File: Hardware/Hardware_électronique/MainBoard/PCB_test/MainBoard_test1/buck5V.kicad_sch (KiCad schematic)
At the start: 12 parts

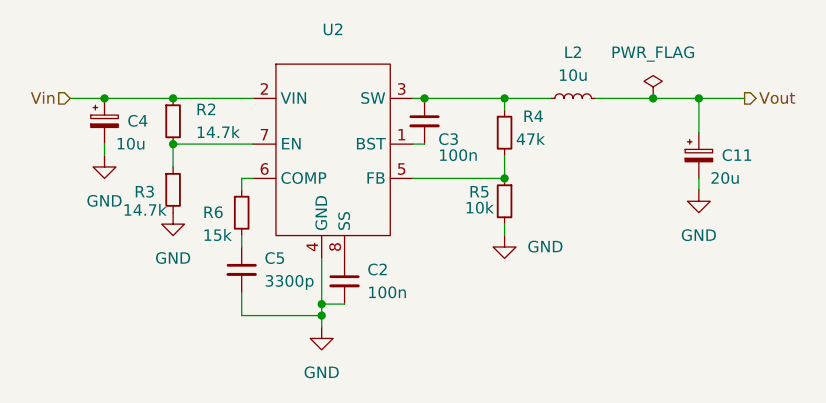
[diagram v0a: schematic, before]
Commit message: finished schematics missing footprints
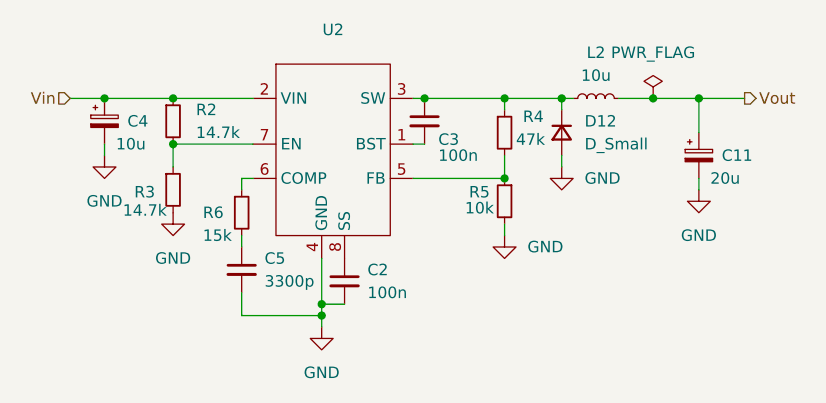
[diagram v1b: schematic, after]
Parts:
- added D12: D_Small, Diode_SMD:D_0603_1608Metric_Pad1.05x0.95mm_HandSolder, symbol Device:D_Small
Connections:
- net GND: now also D12.2 (A)
- net at C3.1, L2.1, R4.1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: now also D12.1 (K)
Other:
- moved on the sheet: L2
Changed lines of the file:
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@@
+	)
+	(junction
+		(at 121.92 63.5)
+		(diameter 0)
+		(color 0 0 0 0)
 	)
 	(junction
@@
 	(wire
 		(pts
+			(xy 121.92 71.12) (xy 121.92 69.85)
+		)
+		(stroke
+			(width 0)
+			(type default)
+		)
+	)
+	(wire
+		(pts
 			(xy 95.25 87.63) (xy 95.25 88.9)
 		)
@@
 	(wire
 		(pts
+			(xy 121.92 64.77) (xy 121.92 63.5)
+		)
+		(stroke
+			(width 0)
+			(type default)
+		)
+	)
+	(wire
+		(pts
 			(xy 105.41 72.39) (xy 115.57 72.39)
 		)
@@
 	(wire
 		(pts
+			(xy 121.92 63.5) (xy 123.19 63.5)
+		)
+		(stroke
+			(width 0)
+			(type default)
+		)
+	)
+	(wire
+		(pts
 			(xy 137.16 73.66) (xy 137.16 72.39)
 		)
@@
 	(wire
 		(pts
-			(xy 115.57 63.5) (xy 120.65 63.5)
+			(xy 115.57 63.5) (xy 121.92 63.5)
 		)
 		(stroke
@@
 	(wire
 		(pts
-			(xy 125.73 63.5) (xy 132.08 63.5)
+			(xy 128.27 63.5) (xy 132.08 63.5)
 		)
 		(stroke
@@
 	(symbol
 		(lib_id "Device:L_Small")
-		(at 123.19 63.5 90)
+		(at 125.73 63.5 90)
 		(unit 1)
 		(exclude_from_sim no)
@@
 		(fields_autoplaced yes)
 		(property "Reference" "L2"
-			(at 123.19 58.42 90)
+			(at 125.73 58.42 90)
 			(effects
 				(font
@@
 		)
 		(property "Value" "10u"
-			(at 123.19 60.96 90)
+			(at 125.73 60.96 90)
 			(effects
 				(font
@@
 		)
 		(property "Footprint" "Inductor_SMD:L_Changjiang_FNR8065S"
-			(at 123.19 63.5 0)
+			(at 125.73 63.5 0)
 			(effects
 				(font
@@
 		)
 		(property "Datasheet" "~"
-			(at 123.19 63.5 0)
+			(at 125.73 63.5 0)
 			(effects
 				(font
@@
 		)
 		(property "Description" ""
-			(at 123.19 63.5 0)
+			(at 125.73 63.5 0)
 			(effects
 				(font
@@
 		)
 		(property "MPN" "74404084220"
-			(at 123.19 63.5 90)
+			(at 125.73 63.5 90)
 			(effects
 				(font
@@
 		)
 		(property "Field5" ""
-			(at 123.19 63.5 90)
+			(at 125.73 63.5 90)
 			(effects
 				(font
@@
 					(unit 1)
 				)
+			)
+		)
+	)
+	(symbol
+		(lib_id "power:GND")
+		(at 121.92 71.12 0)
+		(unit 1)
+		(exclude_from_sim no)
+		(in_bom yes)
+		(on_board yes)
+		(dnp no)
+		(fields_autoplaced yes)
+		(property "Reference" "#PWR028"
+			(at 121.92 77.47 0)
+			(effects
+				(font
+					(size 1.27 1.27)
+				)
+				(hide yes)
+			)
+		)
+		(property "Value" "GND"
+			(at 124.46 72.3899 0)
+			(effects
+				(font
+					(size 1.27 1.27)
+				)
+				(justify left)
+			)
+		)
+		(property "Footprint" ""
+			(at 121.92 71.12 0)
+			(effects
+				(font
+					(size 1.27 1.27)
+				)
+				(hide yes)
+			)
+		)
+		(property "Datasheet" ""
+			(at 121.92 71.12 0)
+			(effects
+				(font
+					(size 1.27 1.27)
+				)
+				(hide yes)
+			)
+		)
+		(property "Description" ""
+			(at 121.92 71.12 0)
+			(effects
+				(font
+					(size 1.27 1.27)
+				)
+				(hide yes)
+			)
+		)
+		(pin "1"
+		)
+		(instances
+			(project "test1"
+				(path "/6efb9aa2-c304-47cb-bf47-2a5d20e826bc/2351e753-aab6-490e-ad96-365a57a146a8"
+					(reference "#PWR028")
+					(unit 1)
+				)
+			)
+		)
+	)
+	(symbol
+		(lib_id "Device:D_Small")
+		(at 121.92 67.31 270)
+		(unit 1)
+		(exclude_from_sim no)
+		(in_bom yes)
+		(on_board yes)
+		(dnp no)
+		(fields_autoplaced yes)
+		(property "Reference" "D12"
+			(at 124.46 66.0399 90)
+			(effects
+				(font
+					(size 1.27 1.27)
+				)
+				(justify left)
+			)
+		)
+		(property "Value" "D_Small"
+			(at 124.46 68.5799 90)
+			(effects
+				(font
+					(size 1.27 1.27)
+				)
+				(justify left)
+			)
+		)
+		(property "Footprint" "Diode_SMD:D_0603_1608Metric_Pad1.05x0.95mm_HandSolder"
+			(at 121.92 67.31 90)
+			(effects
+				(font
+					(size 1.27 1.27)
+				)
+				(hide yes)
+			)
+		)
+		(property "Datasheet" "~"
+			(at 121.92 67.31 90)
+			(effects
+				(font
+					(size 1.27 1.27)
+				)
+				(hide yes)
+			)
+		)
+		(property "Description" "Diode, small symbol"
+			(at 121.92 67.31 0)
+			(effects
+				(font
+					(size 1.27 1.27)
+				)
+				(hide yes)
+			)
+		)
+		(property "Sim.Device" "D"
+			(at 121.92 67.31 0)
+			(effects
+				(font
+					(size 1.27 1.27)
+				)
+				(hide yes)
+			)
+		)
+		(property "Sim.Pins" "1=K 2=A"
+			(at 121.92 67.31 0)
+			(effects
+				(font
+					(size 1.27 1.27)
+				)
+				(hide yes)
+			)
+		)
+		(pin "2"
+		)
+		(pin "1"
+		)
+		(instances
+			(project "test1"
+				(path "/6efb9aa2-c304-47cb-bf47-2a5d20e826bc/2351e753-aab6-490e-ad96-365a57a146a8"
+					(reference "D12")
+					(unit 1)
+				)
